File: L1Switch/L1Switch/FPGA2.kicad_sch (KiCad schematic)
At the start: 46 parts, among them J10 Conn_02x07_Odd_Even, U1 XC7A35T-FTG256, U10 W25Q128JVS, U11 TXB0108PW, U12 TPS386000RGPR

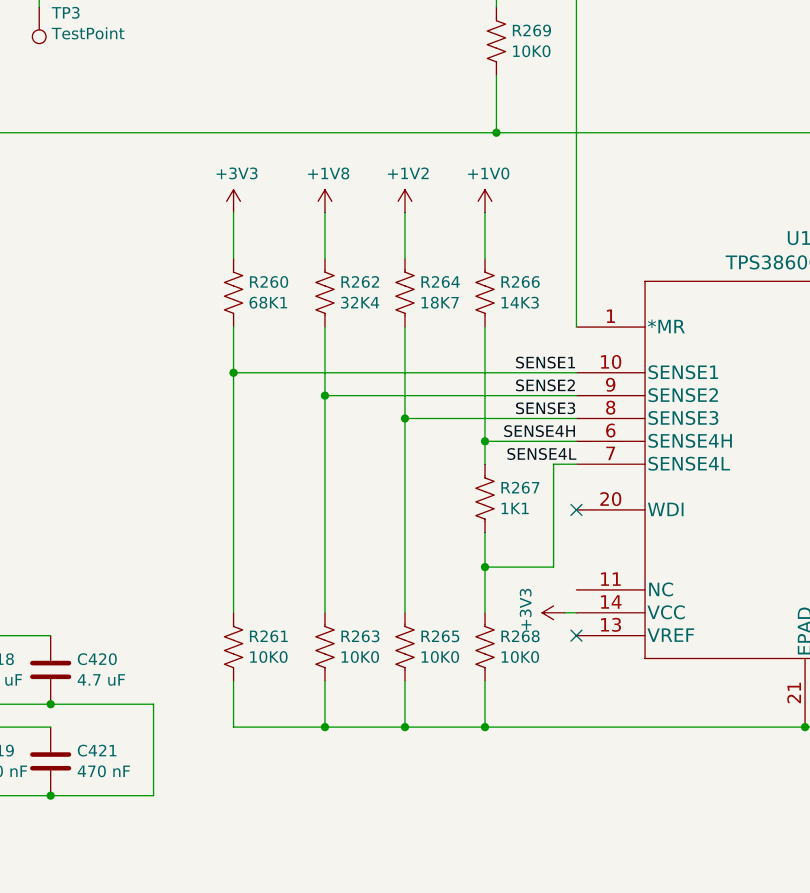
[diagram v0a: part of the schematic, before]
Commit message: Update voltage monitoring.
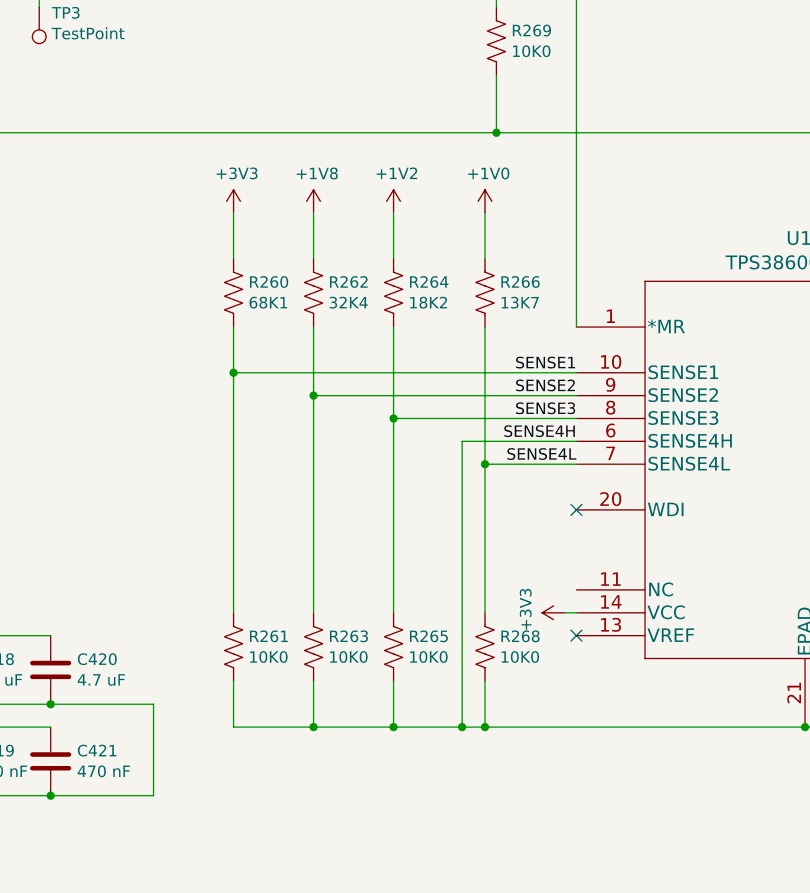
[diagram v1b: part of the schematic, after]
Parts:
- removed R267: 1K1, Resistor_SMD:R_0402_1005Metric, symbol Device:R_US
- R264: value 18K7 -> 18K2
- R266: value 14K3 -> 13K7
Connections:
- net GND: now also U12.6 (SENSE4H)
- net SENSE4L: now also R266.2
- removed net SENSE4H: R266.2, U12.6 (SENSE4H)
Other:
- moved on the sheet: R262, R263, R264, R265
